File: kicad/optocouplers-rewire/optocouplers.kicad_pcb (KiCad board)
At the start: 2 copper layers, 294 x 70 mm, 123 parts, among them Q1 PN2222A, Q2 PN2222A, Q3 PN2222A, Q4 PN2222A, Q5 PN2222A, Q6 PN2222A, Q7 PN2222A, Q8 PN2222A

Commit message: Remove the background drawing of optocouplers
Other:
- board outline removed

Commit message: Move around optocouplers for rows A and C
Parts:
- moved U.A0 16.1 mm to (30.5, 34.5)
- moved U.A1 16.1 mm to (70.5, 34.5)
- moved U.A10 16.1 mm to (210.5, 34.5)
- moved U.A11 16.1 mm to (250.5, 34.5)
- moved U.A2 16.1 mm to (110.5, 34.5)
- moved U.A3 16.1 mm to (150.5, 34.5)
- moved U.A4 16.1 mm to (190.5, 34.5)
- moved U.A5 16.1 mm to (230.5, 34.5)
- moved U.A6 16.1 mm to (50.5, 34.5)
- moved U.A7 16.1 mm to (90.5, 34.5)
- moved U.A8 16.1 mm to (130.5, 34.5)
- moved U.A9 16.1 mm to (170.5, 34.5)
- moved U.C1 7.00 mm to (74.5, 48.5)
- moved U.C10 7.00 mm to (214.5, 48.5)
- moved U.C11 7.00 mm to (254.5, 48.5)
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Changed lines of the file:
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@@
   (net 88 "Net-(R.D10-Pad1)")
   (footprint "ITR9608:ITR9608" (layer "F.Cu")
-    (at 38.5 20.5)
+    (at 30.5 34.5)
     (property "Sheetfile" "optocouplers.kicad_sch")
     (property "Sheetname" "")
@@
   )
   (footprint "ITR9608:ITR9608" (layer "F.Cu")
-    (at 58.5 20.5)
+    (at 50.5 34.5)
     (property "Sheetfile" "optocouplers.kicad_sch")
     (property "Sheetname" "")
@@
   )
   (footprint "ITR9608:ITR9608" (layer "F.Cu")
-    (at 54.5 41.5)
+    (at 54.5 48.5)
     (property "Sheetfile" "optocouplers.kicad_sch")
     (property "Sheetname" "")
@@
   )
   (footprint "ITR9608:ITR9608" (layer "F.Cu")
-    (at 78.5 20.5)
+    (at 70.5 34.5)
     (property "Sheetfile" "optocouplers.kicad_sch")
     (property "Sheetname" "")
@@
   )
   (footprint "ITR9608:ITR9608" (layer "F.Cu")
-    (at 98.5 20.5)
+    (at 90.5 34.5)
     (property "Sheetfile" "optocouplers.kicad_sch")
     (property "Sheetname" "")
@@
   )
   (footprint "ITR9608:ITR9608" (layer "F.Cu")
-    (at 118.5 20.5)
+    (at 110.5 34.5)
     (property "Sheetfile" "optocouplers.kicad_sch")
     (property "Sheetname" "")
@@
   )
   (footprint "ITR9608:ITR9608" (layer "F.Cu")
-    (at 138.5 20.5)
+    (at 130.5 34.5)
     (property "Sheetfile" "optocouplers.kicad_sch")
     (property "Sheetname" "")
@@
   )
   (footprint "ITR9608:ITR9608" (layer "F.Cu")
-    (at 158.5 20.5)
+    (at 150.5 34.5)
     (property "Sheetfile" "optocouplers.kicad_sch")
     (property "Sheetname" "")
@@
   )
   (footprint "ITR9608:ITR9608" (layer "F.Cu")
-    (at 178.5 20.5)
+    (at 170.5 34.5)
     (property "Sheetfile" "optocouplers.kicad_sch")
     (property "Sheetname" "")
@@
   )
   (footprint "ITR9608:ITR9608" (layer "F.Cu")
-    (at 198.5 20.5)
+    (at 190.5 34.5)
     (property "Sheetfile" "optocouplers.kicad_sch")
     (property "Sheetname" "")
@@
   )
   (footprint "ITR9608:ITR9608" (layer "F.Cu")
-    (at 218.5 20.5)
+    (at 210.5 34.5)
     (property "Sheetfile" "optocouplers.kicad_sch")
     (property "Sheetname" "")
@@
   )
   (footprint "ITR9608:ITR9608" (layer "F.Cu")
-    (at 238.5 20.5)
+    (at 230.5 34.5)
     (property "Sheetfile" "optocouplers.kicad_sch")
     (property "Sheetname" "")
@@
   )
   (footprint "ITR9608:ITR9608" (layer "F.Cu")
-    (at 258.5 20.5)
+    (at 250.5 34.5)
     (property "Sheetfile" "optocouplers.kicad_sch")
     (property "Sheetname" "")
@@
   )
   (footprint "ITR9608:ITR9608" (layer "F.Cu")
-    (at 74.5 41.5)
+    (at 74.5 48.5)
     (property "Sheetfile" "optocouplers.kicad_sch")
     (property "Sheetname" "")
@@
   )
   (footprint "ITR9608:ITR9608" (layer "F.Cu")
-    (at 94.5 41.5)
+    (at 94.5 48.5)
     (property "Sheetfile" "optocouplers.kicad_sch")
     (property "Sheetname" "")
@@
   )
   (footprint "ITR9608:ITR9608" (layer "F.Cu")
-    (at 114.5 41.5)
+    (at 114.5 48.5)
     (property "Sheetfile" "optocouplers.kicad_sch")
     (property "Sheetname" "")
@@
   )
   (footprint "ITR9608:ITR9608" (layer "F.Cu")
-    (at 134.5 41.5)
+    (at 134.5 48.5)
     (property "Sheetfile" "optocouplers.kicad_sch")
     (property "Sheetname" "")
@@
   )
   (footprint "ITR9608:ITR9608" (layer "F.Cu")
-    (at 154.5 41.5)
+    (at 154.5 48.5)
     (property "Sheetfile" "optocouplers.kicad_sch")
     (property "Sheetname" "")
@@
   )
   (footprint "ITR9608:ITR9608" (layer "F.Cu")
-    (at 174.5 41.5)
+    (at 174.5 48.5)
     (property "Sheetfile" "optocouplers.kicad_sch")
     (property "Sheetname" "")
@@
   )
   (footprint "ITR9608:ITR9608" (layer "F.Cu")
-    (at 194.5 41.5)
+    (at 194.5 48.5)
     (property "Sheetfile" "optocouplers.kicad_sch")
     (property "Sheetname" "")
@@
   )
   (footprint "ITR9608:ITR9608" (layer "F.Cu")
-    (at 214.5 41.5)
+    (at 214.5 48.5)
     (property "Sheetfile" "optocouplers.kicad_sch")
     (property "Sheetname" "")
@@
   )
   (footprint "ITR9608:ITR9608" (layer "F.Cu")
-    (at 234.5 41.5)
+    (at 234.5 48.5)
     (property "Sheetfile" "optocouplers.kicad_sch")
     (property "Sheetname" "")
@@
   )
   (footprint "ITR9608:ITR9608" (layer "F.Cu")
-    (at 254.5 41.5)
-    (property "Sheetfile" "optocouplers.kicad_sch")
-    (property "Sheetname" "")
+    (at 254.5 48.5)
+    (property "Sheetfile" "optocouplers.kicad_sch")
+    (property "Sheetname" "")

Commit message: Temporary move some resistors around
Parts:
- moved R.A0 21.1 mm to (32.0, 34.5)
- moved R.C0 16.0 mm to (35.5, 48.5), turned to -90 degrees
- moved R.R0 12.0 mm to (44.5, 16.0), turned to 180 degrees
- moved R.B6 10.0 mm to (43.8, 34.5), turned to -90 degrees
- moved R.B0 7.07 mm to (24.0, 34.5), turned to -90 degrees

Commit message: Rename elements on pcb
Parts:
- moved R.A7 21.4 mm to (171.5, 34.5)
- moved R.A9 21.4 mm to (211.5, 34.5)
- moved R.A10 21.1 mm to (232.0, 34.5)
- moved R.A5 21.1 mm to (132.0, 34.5)
- moved R.A6 21.1 mm to (152.0, 34.5)
- moved R.A8 21.1 mm to (192.0, 34.5)
- moved R.A1 21.1 mm to (52.0, 34.5)
- moved R.A2 21.1 mm to (72.0, 34.5)
- moved R.A3 21.1 mm to (92.0, 34.5)
- moved R.A4 21.1 mm to (112.0, 34.5)
- moved R.A11 21.1 mm to (252.0, 34.5)
- moved R.C1 16.1 mm to (56.0, 48.5), turned to -90 degrees
- moved R.C10 16.1 mm to (236.0, 48.5), turned to -90 degrees
- moved R.C2 16.1 mm to (76.0, 48.5), turned to -90 degrees
- moved R.C3 16.1 mm to (96.0, 48.5), turned to -90 degrees
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- renumbered R.A6 to R.A1, R.A5 to R.A10, R.A1 to R.A2, R.A7 to R.A3, R.A2 to R.A4, R.A8 to R.A5, R.A3 to R.A6, R.A9 to R.A7, R.A4 to R.A8, R.A10 to R.A9, R.B5 to R.B10, R.B1 to R.B2, R.B7 to R.B3, R.B2 to R.B4, R.B8 to R.B5, R.B3 to R.B6, R.B9 to R.B7, R.B4 to R.B8, R.B10 to R.B9, R.C6 to R.C1, R.C5 to R.C10, R.C1 to R.C2, R.C7 to R.C3, R.C2 to R.C4, R.C8 to R.C5, R.C3 to R.C6, R.C9 to R.C7, R.C4 to R.C8, R.C10 to R.C9, R.D6 to R.D1, R.D5 to R.D10, R.D1 to R.D2, R.D7 to R.D3, R.D2 to R.D4, R.D8 to R.D5, R.D3 to R.D6, R.D9 to R.D7, R.D4 to R.D8, R.D10 to R.D9, U.A6 to U.A1, U.A5 to U.A10, U.A1 to U.A2, U.A7 to U.A3, U.A2 to U.A4, U.A8 to U.A5, U.A3 to U.A6, U.A9 to U.A7, U.A4 to U.A8, U.A10 to U.A9, U.B6 to U.B1, U.B5 to U.B10, U.B1 to U.B2, U.B7 to U.B3, U.B2 to U.B4, U.B8 to U.B5, U.B3 to U.B6, U.B9 to U.B7, U.B4 to U.B8, U.B10 to U.B9, U.C6 to U.C1, U.C5 to U.C10, U.C1 to U.C2, U.C7 to U.C3, U.C2 to U.C4, U.C8 to U.C5, U.C3 to U.C6, U.C9 to U.C7, U.C4 to U.C8, U.C10 to U.C9, U.D6 to U.D1, U.D5 to U.D10, U.D1 to U.D2, U.D7 to U.D3, U.D2 to U.D4, U.D8 to U.D5, U.D3 to U.D6, U.D9 to U.D7, U.D4 to U.D8, U.D10 to U.D9
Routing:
- net Net-(R.B0-Pad1): track 0.00 -> 3.55 mm
- net Net-(R.A0-Pad1): track 0.00 -> 3.55 mm
- net Net-(R.B6-Pad1): track 0.00 -> 3.45 mm

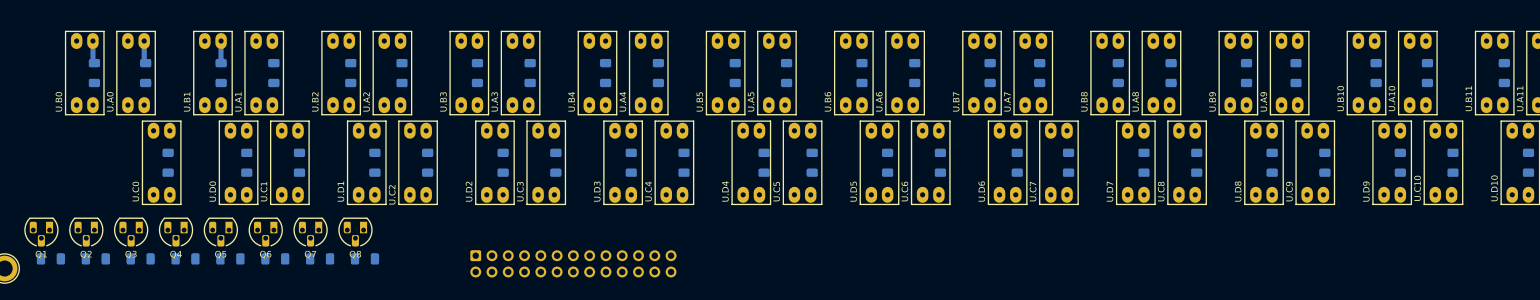
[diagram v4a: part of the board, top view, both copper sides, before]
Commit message: slightly align two resistors, update pcb from schematic, prepare before fixing names of components
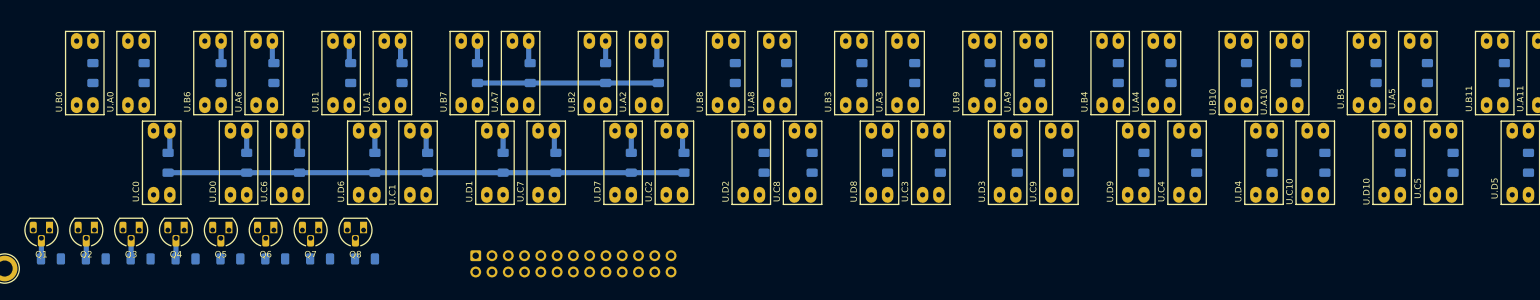
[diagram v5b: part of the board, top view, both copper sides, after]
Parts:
- moved R.A0 0.23 mm to (31.8, 34.5)
- moved R.B0 0.23 mm to (23.8, 34.5)
- renumbered R.A2 to R.A1, R.A9 to R.A10, R.A4 to R.A2, R.A6 to R.A3, R.A8 to R.A4, R.A10 to R.A5, R.A1 to R.A6, R.A3 to R.A7, R.A5 to R.A8, R.A7 to R.A9, R.B2 to R.B1, R.B9 to R.B10, R.B4 to R.B2, R.B6 to R.B3, R.B8 to R.B4, R.B10 to R.B5, R.B3 to R.B7, R.B5 to R.B8, R.B7 to R.B9, R.C2 to R.C1, R.C9 to R.C10, R.C4 to R.C2, R.C6 to R.C3, R.C8 to R.C4, R.C10 to R.C5, R.C1 to R.C6, R.C3 to R.C7, R.C5 to R.C8, R.C7 to R.C9, R.D2 to R.D1, R.D9 to R.D10, R.D4 to R.D2, R.D6 to R.D3, R.D8 to R.D4, R.D10 to R.D5, R.D1 to R.D6, R.D3 to R.D7, R.D5 to R.D8, R.D7 to R.D9, U.A2 to U.A1, U.A9 to U.A10, U.A4 to U.A2, U.A6 to U.A3, U.A8 to U.A4, U.A10 to U.A5, U.A1 to U.A6, U.A3 to U.A7, U.A5 to U.A8, U.A7 to U.A9, U.B2 to U.B1, U.B9 to U.B10, U.B4 to U.B2, U.B6 to U.B3, U.B8 to U.B4, U.B10 to U.B5, U.B1 to U.B6, U.B3 to U.B7, U.B5 to U.B8, U.B7 to U.B9, U.C2 to U.C1, U.C9 to U.C10, U.C4 to U.C2, U.C6 to U.C3, U.C8 to U.C4, U.C10 to U.C5, U.C1 to U.C6, U.C3 to U.C7, U.C5 to U.C8, U.C7 to U.C9, U.D2 to U.D1, U.D9 to U.D10, U.D4 to U.D2, U.D6 to U.D3, U.D8 to U.D4, U.D10 to U.D5, U.D1 to U.D6, U.D3 to U.D7, U.D5 to U.D8, U.D7 to U.D9
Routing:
- net +5V: track 0.00 -> 108.7 mm
- net Net-(R.C0-Pad1): track 0.00 -> 3.56 mm
- net Net-(R.C7-Pad1): track 0.00 -> 3.55 mm
- net Net-(R.C2-Pad1): track 0.00 -> 3.55 mm
- net Net-(R.C1-Pad1): track 0.00 -> 3.55 mm
- net Net-(R.A7-Pad1): track 0.00 -> 3.55 mm
- net Net-(R.A2-Pad1): track 0.00 -> 3.55 mm
- net Net-(R.A1-Pad1): track 0.00 -> 3.55 mm
- net Net-(U.A6-Pad1): track 0.00 -> 3.55 mm
- net Net-(R.C6-Pad1): track 0.00 -> 3.55 mm
- net Net-(R.B1-Pad1): track 0.00 -> 3.55 mm
- net Net-(R.D7-Pad1): track 0.00 -> 3.45 mm
- net Net-(R.D6-Pad1): track 0.00 -> 3.45 mm
- net Net-(R.D1-Pad1): track 0.00 -> 3.45 mm
- net Net-(R.D0-Pad1): track 0.00 -> 3.45 mm
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
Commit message: remove segments
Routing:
- net +5V: track 108.7 -> 0.00 mm
- net Net-(R.C0-Pad1): track 3.56 -> 0.00 mm
- net Net-(R.C7-Pad1): track 3.55 -> 0.00 mm
- net Net-(R.C2-Pad1): track 3.55 -> 0.00 mm
- net Net-(R.C1-Pad1): track 3.55 -> 0.00 mm
- net Net-(R.A7-Pad1): track 3.55 -> 0.00 mm
- net Net-(R.A2-Pad1): track 3.55 -> 0.00 mm
- net Net-(R.A1-Pad1): track 3.55 -> 0.00 mm
- net Net-(U.A6-Pad1): track 3.55 -> 0.00 mm
- net Net-(R.C6-Pad1): track 3.55 -> 0.00 mm
- net Net-(R.B1-Pad1): track 3.55 -> 0.00 mm
- net Net-(R.D7-Pad1): track 3.45 -> 0.00 mm
- net Net-(R.D6-Pad1): track 3.45 -> 0.00 mm
- net Net-(R.D1-Pad1): track 3.45 -> 0.00 mm
- net Net-(R.D0-Pad1): track 3.45 -> 0.00 mm
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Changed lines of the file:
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@@
     )
   )
-  (segment (start 15.73 63.44) (end 15.67 63.5) (width 0.8) (layer "B.Cu") (net 1))
-  (segment (start 15.73 60.27) (end 15.73 63.44) (width 0.8) (layer "B.Cu") (net 1))
-  (segment (start 76 50.05) (end 116 50.05) (width 0.8) (layer "B.Cu") (net 4))
-  (segment (start 83.77 36.05) (end 112 36.05) (width 0.8) (layer "B.Cu") (net 4))
-  (segment (start 35.5 50.05) (end 76 50.05) (width 0.8) (layer "B.Cu") (net 4))
-  (segment (start 22.73 63.44) (end 22.67 63.5) (width 0.8) (layer "B.Cu") (net 20))
-  (segment (start 22.73 60.27) (end 22.73 63.44) (width 0.8) (layer "B.Cu") (net 20))
-  (segment (start 29.73 63.44) (end 29.67 63.5) (width 0.8) (layer "B.Cu") (net 21))
-  (segment (start 29.73 60.27) (end 29.73 63.44) (width 0.8) (layer "B.Cu") (net 21))
-  (segment (start 36.73 63.44) (end 36.67 63.5) (width 0.8) (layer "B.Cu") (net 24))
-  (segment (start 36.73 60.27) (end 36.73 63.44) (width 0.8) (layer "B.Cu") (net 24))
-  (segment (start 31.77 32.72) (end 32 32.95) (width 0.8) (layer "B.Cu") (net 41))
-  (segment (start 71.77 32.72) (end 72 32.95) (width 0.8) (layer "B.Cu") (net 42))
-  (segment (start 71.77 29.5) (end 71.77 32.72) (width 0.8) (layer "B.Cu") (net 42))
-  (segment (start 111.77 29.5) (end 111.77 32.72) (width 0.8) (layer "B.Cu") (net 43))
-  (segment (start 111.77 32.72) (end 112 32.95) (width 0.8) (layer "B.Cu") (net 43))
-  (segment (start 51.77 32.72) (end 52 32.95) (width 0.8) (layer "B.Cu") (net 47))
-  (segment (start 51.77 29.5) (end 51.77 32.72) (width 0.8) (layer "B.Cu") (net 47))
-  (segment (start 91.77 32.72) (end 92 32.95) (width 0.8) (layer "B.Cu") (net 48))
-  (segment (start 91.77 29.5) (end 91.77 32.72) (width 0.8) (layer "B.Cu") (net 48))
-  (segment (start 23.77 32.72) (end 24 32.95) (width 0.8) (layer "B.Cu") (net 53))
-  (segment (start 63.77 32.72) (end 64 32.95) (width 0.8) (layer "B.Cu") (net 54))
-  (segment (start 63.77 29.5) (end 63.77 32.72) (width 0.8) (layer "B.Cu") (net 54))
-  (segment (start 103.77 29.5) (end 103.77 32.95) (width 0.8) (layer "B.Cu") (net 55))
-  (segment (start 43.77 29.5) (end 43.77 32.95) (width 0.8) (layer "B.Cu") (net 59))
-  (segment (start 83.77 29.5) (end 83.77 32.95) (width 0.8) (layer "B.Cu") (net 60))
-  (segment (start 35.77 43.5) (end 35.77 46.68) (width 0.8) (layer "B.Cu") (net 66))
-  (segment (start 35.77 46.68) (end 35.5 46.95) (width 0.8) (layer "B.Cu") (net 66))
-  (segment (start 75.77 43.5) (end 75.77 46.72) (width 0.8) (layer "B.Cu") (net 67))
-  (segment (start 75.77 46.72) (end 76 46.95) (width 0.8) (layer "B.Cu") (net 67))
-  (segment (start 115.77 46.72) (end 116 46.95) (width 0.8) (layer "B.Cu") (net 68))
-  (segment (start 115.77 43.5) (end 115.77 46.72) (width 0.8) (layer "B.Cu") (net 68))
-  (segment (start 55.77 46.72) (end 56 46.95) (width 0.8) (layer "B.Cu") (net 72))
-  (segment (start 55.77 43.5) (end 55.77 46.72) (width 0.8) (layer "B.Cu") (net 72))
-  (segment (start 95.77 43.5) (end 95.77 46.72) (width 0.8) (layer "B.Cu") (net 73))
-  (segment (start 95.77 46.72) (end 96 46.95) (width 0.8) (layer "B.Cu") (net 73))
-  (segment (start 47.77 43.5) (end 47.77 46.95) (width 0.8) (layer "B.Cu") (net 78))
-  (segment (start 87.77 43.5) (end 87.77 46.95) (width 0.8) (layer "B.Cu") (net 79))
-  (segment (start 67.77 43.5) (end 67.77 46.95) (width 0.8) (layer "B.Cu") (net 84))
-  (segment (start 107.77 43.5) (end 107.77 46.95) (width 0.8) (layer "B.Cu") (net 85))
   (zone (net 3) (net_name "GND") (layer "F.Cu") (hatch edge 0.508)
     (connect_pads (clearance 0.508))

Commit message: swap a1 and a6
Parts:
- moved R.A1 20.0 mm to (52.0, 34.5)
- moved R.A6 20.0 mm to (72.0, 34.5)
- moved U.A1 20.0 mm to (50.5, 34.5)
- moved U.A6 20.0 mm to (70.5, 34.5)

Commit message: Fix placements of components for the row A
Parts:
- moved R.A5 100.2 mm to (131.8, 34.5)
- moved U.A5 100.0 mm to (130.5, 34.5)
- moved R.A4 80.2 mm to (111.8, 34.5)
- moved U.A4 80.0 mm to (110.5, 34.5)
- moved U.A6 80.0 mm to (150.5, 34.5)
- moved U.A7 80.0 mm to (170.5, 34.5)
- moved R.A6 79.8 mm to (151.8, 34.5)
- moved R.A7 79.8 mm to (171.8, 34.5)
- moved R.A3 60.2 mm to (91.8, 34.5)
- moved U.A3 60.0 mm to (90.5, 34.5)
- moved U.A8 60.0 mm to (190.5, 34.5)
- moved R.A8 59.8 mm to (191.8, 34.5)
- moved R.A9 40.3 mm to (211.8, 34.5)
- moved R.A2 40.2 mm to (71.8, 34.5)
- moved U.A2 40.0 mm to (70.5, 34.5)
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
